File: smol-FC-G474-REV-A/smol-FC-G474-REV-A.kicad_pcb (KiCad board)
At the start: 2 copper layers, 0 parts

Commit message: Finalized schematic, added power mux
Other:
- board text added: "26x26mm whole size"
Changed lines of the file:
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@@
+		)
+	)
+	(gr_text "26x26mm whole size"
+		(at 197 155.5 0)
+		(layer "F.Fab")
+		(effects
+			(font
+				(size 5 5)
+				(thickness 0.15)
+			)
+			(justify left bottom)
 		)
 	)

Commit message: In progress PCB layout
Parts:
- added 3V3_CORE1: TestPoint, TestPoint:TestPoint_Pad_D1.0mm, B.Cu at (183.1, 81.6)
- added 5V1: TestPoint, pad-2.2x1.6:pad-1.2x1.5, F.Cu at (144.9, 89.1)
- added 5V2: TestPoint, pad-2.2x1.6:pad-1.2x1.5, F.Cu at (149.3, 115.9)
- added 5V3: TestPoint, pad-2.2x1.6:pad-1.2x1.5, F.Cu at (140.9, 113.0)
- added 5V4: TestPoint, pad-2.2x1.6:pad-1.2x1.5, F.Cu at (135.9, 89.1)
- added 5V5: TestPoint, pad-2.2x1.6:pad-1.2x1.5, F.Cu at (157.4, 112.2)
- added 5V6: TestPoint, pad-2.2x1.6:pad-1.2x1.5, F.Cu at (137.3, 113.0)
- added 5V7: TestPoint, pad-2.2x1.6:pad-1.2x1.5, F.Cu at (130.6, 111.5)
- added 9V1: TestPoint, pad-2.2x1.6:pad-1.2x1.5, F.Cu at (134.9, 115.9)
- added AUX1: TestPoint, pad-2.2x1.6:pad-1.2x1.5, F.Cu at (148.6, 89.1)
- added BZ+1: TestPoint, pad-2.2x1.6:pad-1.2x1.5, F.Cu at (152.2, 89.1)
- added BZ-1: TestPoint, pad-2.2x1.6:pad-1.2x1.5, F.Cu at (150.3, 89.1)
- added C1: 100n, Capacitor_SMD:C_0402_1005Metric, B.Cu at (177.5, 128.8)
- added C10: 100n, Capacitor_SMD:C_0402_1005Metric, B.Cu at (126.0, 91.2)
- added C11: 100n, Capacitor_SMD:C_0402_1005Metric, B.Cu at (155.6, 106.9)
- added C12: 10p, Capacitor_SMD:C_0402_1005Metric, B.Cu at (174.1, 129.5)
- added C13: 10p, Capacitor_SMD:C_0402_1005Metric, B.Cu at (172.3, 129.5)
- added C14: 100n, Capacitor_SMD:C_0402_1005Metric, F.Cu at (135.5, 99.9)
- added C15: 100n, Capacitor_SMD:C_0402_1005Metric, F.Cu at (135.5, 102.2)
- added C16: 100n, Capacitor_SMD:C_0402_1005Metric, F.Cu at (144.2, 103.7)
- added C17: 2.2u, Capacitor_SMD:C_0402_1005Metric, F.Cu at (150.1, 98.0)
- added C18: 100n, Capacitor_SMD:C_0402_1005Metric, F.Cu at (149.1, 98.0)
- added C19: 10n, Capacitor_SMD:C_0402_1005Metric, F.Cu at (146.5, 99.2)
- added C2: 100n, Capacitor_SMD:C_0402_1005Metric, B.Cu at (174.0, 117.9)
- added C20: 100n, Capacitor_SMD:C_0402_1005Metric, F.Cu at (134.3, 99.8)
- added C21: 47u, Capacitor_SMD:C_1206_3216Metric, F.Cu at (138.3, 109.4)
- added C22: 47u, Capacitor_SMD:C_1206_3216Metric, F.Cu at (138.3, 107.0)
- added C23: 10p, Capacitor_SMD:C_0402_1005Metric, F.Cu at (144.1, 109.6)
- added C24: 10p, Capacitor_SMD:C_0402_1005Metric, F.Cu at (146.6, 107.5)
- added C25: 100n, Capacitor_SMD:C_0402_1005Metric, F.Cu at (169.9, 104.0)
- added C26: 100n, Capacitor_SMD:C_0402_1005Metric, F.Cu at (148.4, 103.6)
- added C27: 100n, Capacitor_SMD:C_0402_1005Metric, F.Cu at (150.1, 101.5)
- added C28: 4.7u, Capacitor_SMD:C_0402_1005Metric, F.Cu at (141.7, 92.6)
- added C29: 4.7u, Capacitor_SMD:C_0805_2012Metric, B.Cu at (136.7, 96.3)
- added C3: 100n, Capacitor_SMD:C_0402_1005Metric, B.Cu at (188.4, 125.4)
- added C30: 47u, Capacitor_SMD:C_0805_2012Metric, B.Cu at (136.9, 100.0)
- added C31: 47u, Capacitor_SMD:C_0805_2012Metric, B.Cu at (137.0, 103.4)
- added C32: 10u, Capacitor_SMD:C_0402_1005Metric, B.Cu at (221.8, 81.1)
- added C33: 1u, Capacitor_SMD:C_0402_1005Metric, B.Cu at (221.8, 83.1)
- added C34: 1u, Capacitor_SMD:C_0603_1608Metric, B.Cu at (131.5, 97.9)
- added C35: 10u, Capacitor_SMD:C_0402_1005Metric, B.Cu at (221.8, 85.1)
- added C36: 1u, Capacitor_SMD:C_0402_1005Metric, B.Cu at (221.8, 87.0)
- added C37: 4.7u, Capacitor_SMD:C_0805_2012Metric, B.Cu at (118.0, 101.5)
- added C38: 22u, Capacitor_SMD:C_0805_2012Metric, B.Cu at (118.6, 108.0)
- added C39: 1u, Capacitor_SMD:C_0603_1608Metric, B.Cu at (111.8, 103.2)
- added C4: 100n, Capacitor_SMD:C_0402_1005Metric, B.Cu at (185.8, 115.4)
- added C40: 10u, Capacitor_SMD:C_0402_1005Metric, B.Cu at (221.8, 91.0)
- added C41: 10u, Capacitor_SMD:C_0402_1005Metric, B.Cu at (221.8, 89.0)
- added C42: 10u, Capacitor_SMD:C_0402_1005Metric, B.Cu at (221.8, 94.9)
- added C43: 10u, Capacitor_SMD:C_0402_1005Metric, B.Cu at (221.8, 93.0)
- added C5: 4.7u, Capacitor_SMD:C_0402_1005Metric, B.Cu at (173.1, 117.9)
- added C6: 1u, Capacitor_SMD:C_0402_1005Metric, B.Cu at (182.9, 113.6)
- added C7: 100n, Capacitor_SMD:C_0402_1005Metric, B.Cu at (182.9, 114.5)
- added C8: 100n, Capacitor_SMD:C_0402_1005Metric, B.Cu at (173.6, 122.4)
- added C9: 100n, Capacitor_SMD:C_0402_1005Metric, B.Cu at (126.0, 90.1)
- added CAM1: TestPoint, pad-2.2x1.6:pad-1.2x1.5, F.Cu at (139.6, 89.1)
- added CC1: TestPoint, pad-2.2x1.6:pad-1.2x1.5, F.Cu at (143.2, 89.1)
- added CURR1: TestPoint, pad-2.2x1.6:pad-1.2x1.5, B.Cu at (141.0, 89.0)
- added D1: LED, LED_SMD:LED_0603_1608Metric, F.Cu at (131.7, 98.8)
- added D2: LED, LED_SMD:LED_0603_1608Metric, F.Cu at (131.7, 97.3)
- added D3: ESD, ESDALC6V1-1U2:DIODE_ESDALC6V1-1U2, F.Cu at (131.9, 108.0)
- added D4: RED, LED_SMD:LED_0603_1608Metric, F.Cu at (131.7, 95.8)
- added GND1: TestPoint, TestPoint:TestPoint_Pad_D1.0mm, B.Cu at (183.1, 84.6)
- added GND10: TestPoint, pad-2.2x1.6:pad-1.2x1.5, F.Cu at (130.6, 109.8)
- added GND11: TestPoint, pad-2.2x1.6:pad-1.2x1.5, F.Cu at (143.9, 115.9)
- added GND2: TestPoint, pad-2.2x1.6:pad-1.2x1.5, F.Cu at (146.8, 89.1)
- added GND3: TestPoint, pad-2.2x1.6:pad-1.2x1.5, F.Cu at (147.6, 115.9)
- added GND4: TestPoint, pad-2.2x1.6:pad-1.2x1.5, B.Cu at (139.0, 89.0)
- added GND5: TestPoint, pad-2.2x1.6:pad-1.2x1.5, F.Cu at (139.1, 113.0)
- added GND6: TestPoint, pad-2.2x1.6:pad-1.2x1.5, F.Cu at (137.8, 89.1)
- added GND7: TestPoint, pad-2.2x1.6:pad-1.2x1.5, F.Cu at (136.8, 115.9)
- added GND8: TestPoint, pad-2.2x1.6:pad-1.2x1.5, F.Cu at (141.3, 89.1)
- added GND9: TestPoint, pad-2.2x1.6:pad-1.2x1.5, F.Cu at (157.4, 108.7)
- added I2C3_SCL1: TestPoint, pad-2.2x1.6:pad-1.2x1.5, F.Cu at (148.1, 113.0)
- added I2C3_SDA1: TestPoint, pad-2.2x1.6:pad-1.2x1.5, F.Cu at (149.9, 113.0)
- added J1: ESC, Connector_JST:JST_SH_SM10B-SRSS-TB_1x10-1MP_P1.00mm_Horizontal, B.Cu at (144.7, 92.6)
- added L1: 1.5u, inductor:IND-SMD_L3.0-W3.0_YSMC0320H, B.Cu at (134.2, 101.2)
- added L2: 3.3u, inductor:APH0430C-3R3M-TCD5, B.Cu at (117.2, 105.0)
- added LED1: TestPoint, pad-2.2x1.6:pad-1.2x1.5, F.Cu at (157.4, 110.5)
- added M1: TestPoint, pad-2.2x1.6:pad-1.2x1.5, B.Cu at (145.0, 89.0)
- added M2: TestPoint, pad-2.2x1.6:pad-1.2x1.5, B.Cu at (147.0, 89.0)
- added M3: TestPoint, pad-2.2x1.6:pad-1.2x1.5, B.Cu at (149.0, 89.0)
- added M4: TestPoint, pad-2.2x1.6:pad-1.2x1.5, B.Cu at (151.0, 89.0)
- added Q1: BC817W, Package_TO_SOT_SMD:SOT-323_SC-70, F.Cu at (150.0, 92.8)
- added R1: 1k, Resistor_SMD:R_0402_1005Metric, F.Cu at (130.7, 100.5)
- added R10: 5.1k, Resistor_SMD:R_0402_1005Metric, F.Cu at (150.9, 99.8)
- added R11: 75, Resistor_SMD:R_0402_1005Metric, F.Cu at (134.8, 98.4)
- added R12: 75, Resistor_SMD:R_0402_1005Metric, F.Cu at (141.1, 109.6)
- added R13: 10K, Resistor_SMD:R_0402_1005Metric, F.Cu at (169.8, 106.1)
- added R14: 4.7k, Resistor_SMD:R_0402_1005Metric, F.Cu at (146.2, 101.4)
- added R15: 4.7k, Resistor_SMD:R_0402_1005Metric, F.Cu at (146.2, 100.4)
- added R16: 330, Resistor_SMD:R_0402_1005Metric, F.Cu at (143.1, 92.1)
- added R17: 4.7k, Resistor_SMD:R_0402_1005Metric, B.Cu at (194.3, 112.9)
- added R18: 4.7k, Resistor_SMD:R_0402_1005Metric, B.Cu at (194.3, 110.9)
- added R19: 1k, Resistor_SMD:R_0402_1005Metric, F.Cu at (148.2, 93.2)
- added R2: 1k, Resistor_SMD:R_0402_1005Metric, F.Cu at (131.6, 100.5)
- added R20: 10k, Resistor_SMD:R_0402_1005Metric, B.Cu at (224.7, 89.1)
- added R21: 7.15k, Resistor_SMD:R_0402_1005Metric, B.Cu at (131.5, 95.0)
- added R22: 10k, Resistor_SMD:R_0402_1005Metric, B.Cu at (224.7, 91.1)
- added R23: 80.6k, Resistor_SMD:R_0402_1005Metric, B.Cu at (126.3, 106.8)
- added R24: 10k, Resistor_SMD:R_0402_1005Metric, B.Cu at (126.7, 104.0)
- added R25: 100k, Resistor_SMD:R_0402_1005Metric, B.Cu at (224.7, 93.1)
- added R26: 10k, Resistor_SMD:R_0402_1005Metric, B.Cu at (112.1, 100.2)
- added R27: 39k, Resistor_SMD:R_0402_1005Metric, B.Cu at (224.7, 95.1)
- added R3: 100k, Resistor_SMD:R_0402_1005Metric, B.Cu at (197.1, 86.2)
- added R4: 10k, Resistor_SMD:R_0402_1005Metric, B.Cu at (197.2, 83.8)
- added R5: 10k, Resistor_SMD:R_0402_1005Metric, F.Cu at (132.2, 107.1)
- added R6: 100k, Resistor_SMD:R_0402_1005Metric, B.Cu at (155.8, 100.3)
- added R7: 100k, Resistor_SMD:R_0402_1005Metric, B.Cu at (154.9, 100.3)
- added R8: 1k, Resistor_SMD:R_0402_1005Metric, F.Cu at (132.6, 100.5)
- added R9: 5.1k, Resistor_SMD:R_0402_1005Metric, F.Cu at (150.9, 104.4)
- added RX1: TestPoint, pad-2.2x1.6:pad-1.2x1.5, F.Cu at (145.8, 115.9)
- added RX2: TestPoint, pad-2.2x1.6:pad-1.2x1.5, F.Cu at (140.3, 115.9)
- added RX3: TestPoint, pad-2.2x1.6:pad-1.2x1.5, F.Cu at (152.9, 115.9)
- added RX4: TestPoint, pad-2.2x1.6:pad-1.2x1.5, F.Cu at (144.5, 113.0)
- added SW1: BOOT, B3U-1000P:KEY-SMD_B3U-1000PM, F.Cu at (131.7, 104.5)
- added SWCLK1: TestPoint, TestPoint:TestPoint_Pad_D1.0mm, B.Cu at (183.1, 87.6)
- added SWDIO1: TestPoint, TestPoint:TestPoint_Pad_D1.0mm, B.Cu at (183.1, 90.7)
- added TEL1: TestPoint, pad-2.2x1.6:pad-1.2x1.5, B.Cu at (143.0, 89.0)
- added TX1: TestPoint, pad-2.2x1.6:pad-1.2x1.5, F.Cu at (146.3, 113.0)
- added TX2: TestPoint, pad-2.2x1.6:pad-1.2x1.5, F.Cu at (142.2, 115.9)
- added TX3: TestPoint, pad-2.2x1.6:pad-1.2x1.5, F.Cu at (151.2, 115.9)
- added TX4: TestPoint, pad-2.2x1.6:pad-1.2x1.5, F.Cu at (142.7, 113.0)
- added U1: STM32G474RETx, Package_QFP:LQFP-64_10x10mm_P0.5mm, B.Cu at (146.8, 103.9)
- added U10: LP5912-3.3DRV, Package_SON:WSON-6-1EP_2x2mm_P0.65mm_EP1x1.6mm, B.Cu at (213.6, 96.4)
- added U11: LMQ66430R5RXBR, LMQ66430:RXB0014A-MFG, B.Cu at (132.7, 106.2)
- added U12: TPS2116DRL, Package_TO_SOT_SMD:SOT-583-8, B.Cu at (208.8, 87.2)
- added U2: USBLC6-2P6, Package_TO_SOT_SMD:SOT-666, B.Cu at (155.7, 104.5)
- added U3: ICM-42688-P, ICM-42688-P:PQFN50P300X250X97-14N, F.Cu at (146.9, 97.2)
- added U4: AT7456E, AT7456E:SOP65P637X110-28N, F.Cu at (139.9, 100.8)
- added U5: W25Q128JVSIQ, W25Q128JVSIQ:SOIC127P790X216-8N, F.Cu at (175.1, 103.6)
- added U6: DPS368XTSA1, DPS368XTSA1:XDCR_DPS368XTSA1, F.Cu at (148.4, 101.5)
- added U7: TVS3300DRVR, TVS3300DRVR:DRV6_1X1P6_TEX, B.Cu at (140.4, 96.9)
- added U8: LMQ66430R5RXBR, LMQ66430:RXB0014A-MFG, B.Cu at (134.1, 97.2)
- added U9: LP5912-3.3DRV, Package_SON:WSON-6-1EP_2x2mm_P0.65mm_EP1x1.6mm, B.Cu at (213.6, 92.7)
- added USB1: TYPE-C 16P QTWT, USB-C-SMD:USB-TYPE-C-SMD_TYPE-C-16P-QTWT, F.Cu at (155.1, 101.5)
- added VBAT1: TestPoint, pad-2.2x1.6:pad-1.2x1.5, B.Cu at (137.0, 89.0)
- added VIDEO_OUT1: TestPoint, pad-2.2x1.6:pad-1.2x1.5, F.Cu at (138.6, 115.9)
- added Y1: 8MHz, NX3225GD:XTAL_NX3225GD-8MHZ-STD-CRA-3, B.Cu at (173.2, 127.4)
- added Y2: 27MHz, SX1B27.000F0810F30:XTAL_TSX-3225_16.0000MF18X-AC3, F.Cu at (144.1, 107.5)
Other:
- board outline added: 29 x 29 mm
- copper layers 2 -> 6
- board text added: "1"
- board text added: "2"
- board text added: "3"
- board text added: "4"
- board text added: "C"
- board text added: "G"
- board text added: "PLACE ME SENPAI! >_<"
- board text added: "T"
- board text added: "V"
- board text removed: "26x26mm whole size"

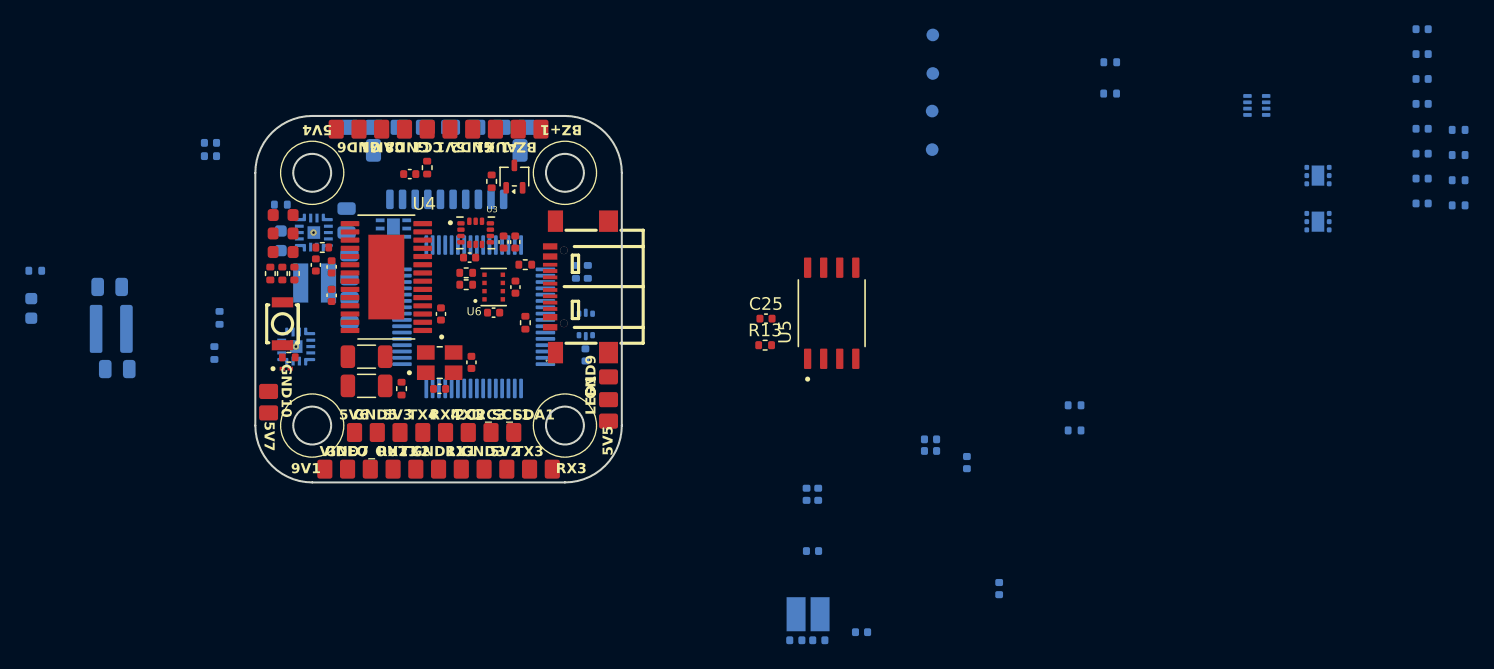
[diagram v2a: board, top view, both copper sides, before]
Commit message: changed size of cap on buck's
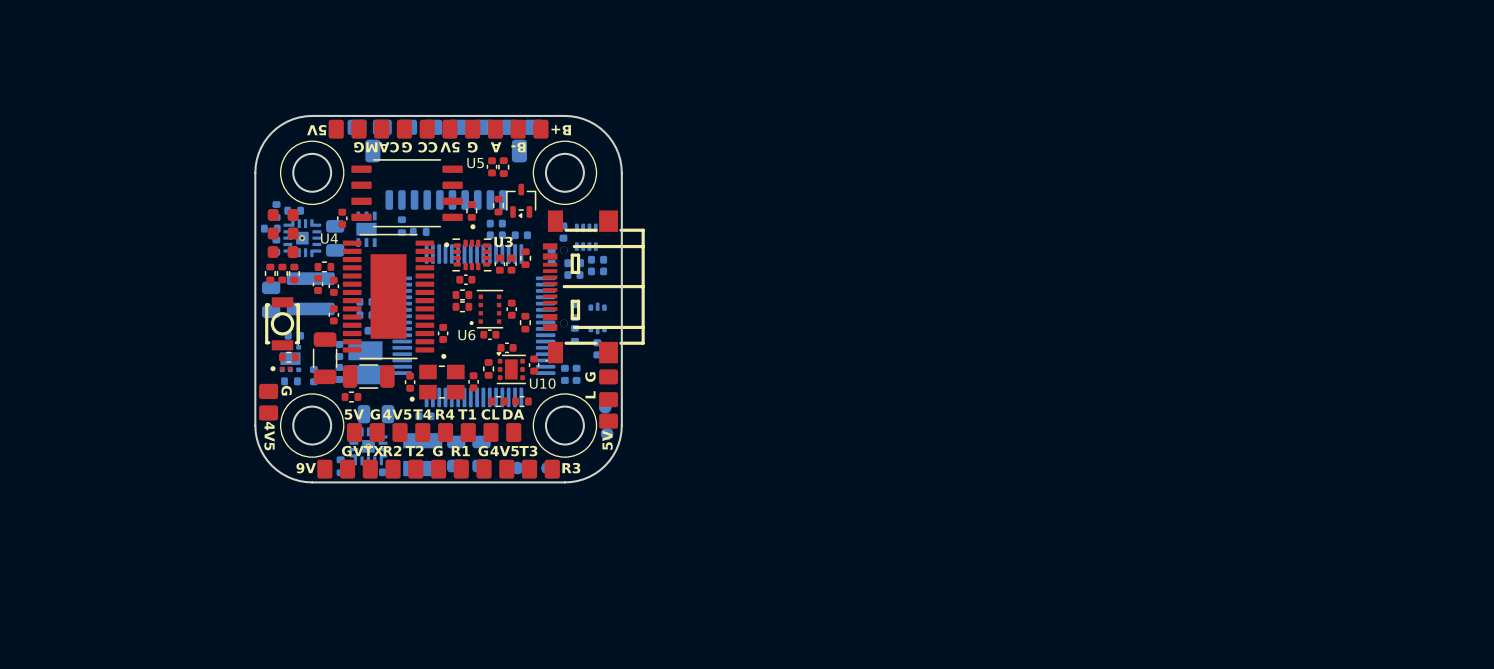
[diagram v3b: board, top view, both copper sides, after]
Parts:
- C29, C37: value 4.7u -> 3.3u
- C34, C39: footprint Capacitor_SMD:C_0603_1608Metric -> Capacitor_SMD:C_0402_1005Metric
- C35, C36, R17, R18, R22, U10: moved to F.Cu
- moved R20 94.5 mm to (132.3, 109.0)
- moved C32 92.5 mm to (132.6, 105.4)
- moved C33 91.3 mm to (134.1, 108.5), turned to 90 degrees
- moved U9 82.6 mm to (132.3, 107.2), turned to 90 degrees
- moved R22 78.6 mm to (148.0, 108.0), turned to -90 degrees
- moved C36 74.9 mm to (149.4, 106.3), turned to 0 degrees
- moved C35 73.8 mm to (151.6, 107.7), turned to -90 degrees
- moved R27 71.9 mm to (152.9, 99.1), turned to 90 degrees
- moved R25 70.3 mm to (154.7, 99.7)
- moved C43 68.1 mm to (153.9, 97.2), turned to -90 degrees
- moved C42 67.4 mm to (154.7, 100.6)
- moved C41 66.1 mm to (156.6, 99.4), turned to 0 degrees
- moved C40 65.9 mm to (156.6, 100.3), turned to 0 degrees
- moved U10 64.9 mm to (149.8, 108.1), turned to 0 degrees
- moved R3 57.0 mm to (141.1, 96.7), turned to -90 degrees
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- renumbered 3V3_CORE1 to 3V3, 5V2 to 4V5, 5V7 to 4V5, 5V3 to 4V5, 5V6 to 5V, 5V4 to 5V, 5V5 to 5V, 5V1 to 5V, 9V1 to 9V, AUX1 to A, BZ+1 to B+, BZ-1 to B-, CAM1 to CAM, CC1 to CC, I2C3_SCL1 to CL, SWCLK1 to CLK, I2C3_SDA1 to DA, SWDIO1 to DIO, J1 to ESC, GND3 to G, GND1 to G, GND2 to G, GND11 to G, GND9 to G, GND7 to G, GND6 to G, GND10 to G, GND5 to G, GND8 to G, LED1 to L, RX1 to R1, RX2 to R2, RX3 to R3, RX4 to R4, TX1 to T1, TX2 to T2, TX3 to T3, TX4 to T4, VIDEO_OUT1 to VTX
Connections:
- C28 pad 1: /Connectors/CC -> /Connectors/CC_P
- CC pad 1: /Connectors/CC -> /Connectors/CC_P
- R16 pad 2: /Connectors/CC -> /Connectors/CC_P
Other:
- board text added: "PLACE ME SENPAI! ( >_< )"
- board text removed: "PLACE ME SENPAI! >_<"

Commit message: Opis Twoich zmian
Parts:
- moved R1 6.57 mm to (124.3, 99.0)
- moved R8 6.57 mm to (126.2, 99.0)
- moved D1 6.57 mm to (125.3, 97.3)
- moved D2 6.57 mm to (125.3, 95.8)
- moved D4 6.57 mm to (125.3, 94.3)
- moved R2 6.57 mm to (125.2, 99.0)
- moved R4 5.28 mm to (138.2, 100.3), turned to 90 degrees
- moved R3 5.22 mm to (137.3, 100.3)
- moved C43 2.52 mm to (156.0, 95.8), turned to 0 degrees
- moved U7 2.30 mm to (140.6, 96.9), turned to 180 degrees
- moved R11 1.43 mm to (133.8, 100.8), turned to 180 degrees
- moved R27 0.88 mm to (152.9, 98.2)
- moved C20 0.82 mm to (134.3, 102.1)
- moved DIO 0.72 mm to (153.3, 116.0)
- moved CLK 0.72 mm to (150.9, 116.0)
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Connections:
- net Net-(C21-Pad2) renamed /Sensors & IC's/V_OUT
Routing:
- net /MCU/MCU_USB_D_P: track 0.00 -> 7.20 mm
- net /MCU/HSE_IN: track 0.00 -> 6.35 mm
- net /MCU/ADC_VBAT: track 0.00 -> 5.61 mm
- net /MCU/MCU_USB_D_N: track 0.00 -> 5.50 mm
- net /MCU/HSE_OUT: track 0.00 -> 4.78 mm
- net +VBAT: track 0.00 -> 4.48 mm, vias 0 -> 3
- net /MCU/USB_SENS: track 0.00 -> 4.02 mm
- net /Power Supply/MUX_PR1: track 0.00 -> 3.78 mm
- net /MCU/NRST: track 0.00 -> 1.89 mm
- net +5V_BEC: track 0.00 -> 1.69 mm, vias 0 -> 2
- net /Power Supply/Buck-9V_FB: track 0.00 -> 0.91 mm
- net GND: vias 0 -> 24
- net +VBUS: vias 0 -> 3
- net +9V_BEC: vias 0 -> 3
- net +5V_SYS: vias 0 -> 2
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- added copper zone on B.Cu, net +3V3_CORE
- added copper zone on B.Cu, net +5V_BEC
- added copper zone on B.Cu, net +5V_SYS
- added copper zone on B.Cu, net +9V_BEC
- added copper zone on B.Cu, net +VBAT
- added copper zone on B.Cu, net +VBUS
- added copper zone on B.Cu, net /Power Supply/Buck-9V_FB
- added copper zone on B.Cu, net /Power Supply/Buck-9V_RT
- added copper zone on B.Cu, net /Power Supply/Buck-9V_SW
- added copper zone on B.Cu, net /Power Supply/Buck-9V_VCC_INT
- added copper zone on B.Cu, net GND
